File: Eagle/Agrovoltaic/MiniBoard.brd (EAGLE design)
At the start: 160 x 100 mm, 56 parts, among them J1 WAGO-03BE, J2 WAGO-03BE, J3 WAGO-03BE, K1 SRD-05VDC-SL-C, K3 SRD-05VDC-SL-C, Q1 BC338, Q2 BC338

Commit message: EDIT:Mengedit Board
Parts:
- removed CA3: 100n, rcl:E3,5-8
- removed MC1: DEVKIT_V1_ESP32-WROOM-32, DEVKIT_V1_ESP32-WROOM-32:MODULE_DEVKIT_V1_ESP32-WROOM-32
- added ANALOG, DIGITAL-IN, DIGITAL-OUT: (no value), con-wago-500:W237-102
- added CA4: 100n, rcl:E3,5-8
- added U$1: CP8-ADJ, userlib:CP8-ADJ
- added U1: ESP32-DEVKIT-V1, ESP32-DEVKIT-V1:MODULE_ESP32_DEVKIT_V1
- added UART2: 332-02, con-garry:332-02
- R12, R14: value 3K -> 2K
- R25, R26: value 3K -> 180
- moved K3 199.5 mm to (88.9, 125.7)
- moved K1 194.1 mm to (88.9, 142.2)
- moved OK3 187.4 mm to (88.9, 16.5), turned to 270 degrees
- moved R19 182.3 mm to (73.7, 26.7), turned to 180 degrees
- moved D14 177.6 mm to (87.6, 34.3), turned to 180 degrees
- moved J3 174.3 mm to (104.1, 120.7), turned to 90 degrees
- moved DZA1 165.6 mm to (73.7, 78.7)
- moved J2 163.7 mm to (104.1, 137.2), turned to 90 degrees
- moved CA2 161.6 mm to (86.4, 104.1)
- moved R14 158.8 mm to (76.2, 58.4), turned to 180 degrees
- moved I2C 155.6 mm to (57.1, 5.08)
- moved RA13 154.3 mm to (67.3, 88.9)
- moved D13 154.0 mm to (73.7, 30.5), turned to 180 degrees
- moved D3 153.5 mm to (71.1, 119.4)
- moved R1 152.9 mm to (73.7, 14.0), turned to 180 degrees
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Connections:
- removed net IO16: MC1.27
- removed net IO17: MC1.28
- removed net IO4: MC1.26
- removed net N$10: IOESP.4
- removed net N$11: IOESP.5
- removed net N$12: IOESP.6
- removed net N$13: IOESP.7
- removed net N$14: IOESP.8
- removed net N$23: CA3.+, MC1.2
- removed net N$44: MC1.16
- removed net N$45: MC1.17
- removed net N$46: MC1.18
- removed net N$5: IOESP.1
- removed net N$61: MC1.25
- removed net N$64: MC1.22
- removed net N$65: MC1.21
- removed net N$66: MC1.20
- removed net N$8: IOESP.2
- removed net N$9: IOESP.3
- removed net R3: MC1.13
- removed net R4: MC1.15
- removed net S3: MC1.9
- removed net S4: MC1.10
- new net AI2: ANALOG.2, CA2.+, DZA3.A, DZA4.C, RA21.2
- new net D12: IOESP.3, U1.27
- new net D13: IOESP.4, U1.28
- new net D25: IOESP.5, U1.23
- new net D26: IOESP.6, U1.24
- new net D4: IOESP.1, U1.5
- new net D5: IOESP.2, U1.8
- new net N$25: CA4.+, U1.16
- new net RX2: U1.6, UART2.2
- new net TX2: U1.7, UART2.1
- net 12V: now also J1.3, U$1.IN+; no longer J1.1
- net 3V3: now also U1.1; no longer MC1.1
- net 5V: now also U$1.OUT+, U1.30; no longer MC1.19
- net A1: now also U1.21; no longer MC1.7, RA21.1, RA22.2, RA23.2
- net A2: now also RA21.1, RA22.2, RA23.2, U1.22; no longer MC1.8
- net AI1: now also ANALOG.1; no longer CA2.+, DZA3.A, DZA4.C, RA21.2
- net CS: no longer MC1.29
- net GND: now also CA4.-, J1.1, U$1.IN-, U$1.OUT-, U1.2, U1.29; no longer CA3.-, J1.3, MC1.14, MC1.32, MC1.38
- net IN1: now also DIGITAL-IN.1
- net IN2: now also DIGITAL-IN.2
- net MISO: now also U1.10; no longer MC1.31
- net MOSI: now also U1.15; no longer MC1.37
- net OUT1: now also DIGITAL-OUT.1
- net OUT2: now also DIGITAL-OUT.2
- net R1: now also U1.25; no longer MC1.11
- net R2: now also U1.26; no longer MC1.12
- net RR1: now also U1.3; no longer MC1.23
- net RR2: now also U1.4; no longer MC1.24
- net RX0: now also U1.12; no longer MC1.34
- net S1: now also U1.19; no longer MC1.5
- net S2: now also U1.20; no longer MC1.6
- net SCK: now also U1.9; no longer MC1.30
- net SCL: now also U1.14; no longer MC1.36
- net SDA: now also U1.11; no longer MC1.33
- net TX0: now also U1.13; no longer MC1.35
- net VN: now also IOESP.8, U1.18; no longer MC1.4
- net VP: now also IOESP.7, U1.17; no longer MC1.3
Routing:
- net RX0: track 0.00 -> 2.81 mm
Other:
- board size 160 x 100 mm -> 108 x 151.1 mm

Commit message: EDIT:Melanjutkan
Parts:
- added SV1, SV2, SV3, SV4, SV5, SV6, SV7, SV8: (no value), con-lsta:FE10
- moved UART 40.3 mm to (55.9, 41.9), turned to 180 degrees
- moved UART2 29.8 mm to (55.9, 26.7), turned to 180 degrees
- moved R13 24.4 mm to (50.8, 82.5), turned to 270 degrees
- moved R26 24.3 mm to (33.0, 83.8)
- moved OK7 24.2 mm to (43.2, 82.5)
- moved OLED_LCD 23.0 mm to (26.7, 73.7), turned to 270 degrees
- moved CA4 19.1 mm to (29.2, 40.6), turned to 270 degrees
- moved U1 17.8 mm to (33.0, 27.9)
- moved R25 16.7 mm to (33.0, 63.5)
- moved OK6 16.6 mm to (43.2, 62.2)
- moved SPI 15.3 mm to (55.9, 16.5)
- moved R11 13.3 mm to (50.8, 62.2), turned to 90 degrees
- moved R20 7.73 mm to (72.4, 41.9)
- moved RA22 7.62 mm to (59.7, 108.0)
- moved RA23 7.62 mm to (59.7, 101.6)
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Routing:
- net 5V: track 0.00 -> 246.8 mm
- net GND: track 0.00 -> 246.5 mm
- net AI1: track 0.00 -> 43.6 mm
- net N$6: track 0.00 -> 42.7 mm
- net N$3: track 0.00 -> 42.5 mm
- net AI2: track 0.00 -> 41.3 mm
- net N$19: track 0.00 -> 26.5 mm
- net OUT2: track 0.00 -> 25.8 mm
- net COM2: track 0.00 -> 23.3 mm
- net COM1: track 0.00 -> 23.3 mm
- net 12V: track 0.00 -> 18.6 mm
- net N$4: track 0.00 -> 18.0 mm
- net OUT1: track 0.00 -> 17.3 mm
- net N$7: track 0.00 -> 16.7 mm
- net N$25: track 0.00 -> 11.2 mm
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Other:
- board text added: "Button"

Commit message: Still Edit
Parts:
- added RA1, RA2, RA3, RA4, RA5: 10K, rcl:0207/10
- added S1, S2, S3: FSM103A, FSM103A:SW_1571627-1
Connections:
- new net N$5: RA1.2, RA5.1, S1.1, S1.2
- new net N$8: RA1.1, RA2.2, S2.1, S2.2
- new net N$9: RA2.1, RA3.2, S3.1, S3.2
- net 3V3: now also RA5.2
- net CS: now also U1.8
- net D4: now also RA4.2, S1.3, S1.4, S2.3, S2.4, S3.3, S3.4
- net D5: no longer U1.8
- net GND: now also RA3.1, RA4.1
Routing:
- net SCL: track 0.00 -> 53.4 mm
- net SDA: track 0.00 -> 46.6 mm
- net N$8: track 0.00 -> 33.0 mm
- net MISO: track 0.00 -> 30.4 mm
- net D4: track 0.00 -> 29.9 mm
- net SCK: track 0.00 -> 27.2 mm
- net N$5: track 0.00 -> 23.8 mm
- net N$9: track 0.00 -> 22.7 mm
- net 12V: track 18.6 -> 40.6 mm
- net GND: track 246.5 -> 266.6 mm
- net N$19: track 26.5 -> 38.1 mm
- net RX2: track 0.00 -> 10.4 mm
- net RX0: track 0.00 -> 10.4 mm
- net TX2: track 0.00 -> 10.2 mm
- net TX0: track 0.39 -> 10.5 mm
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
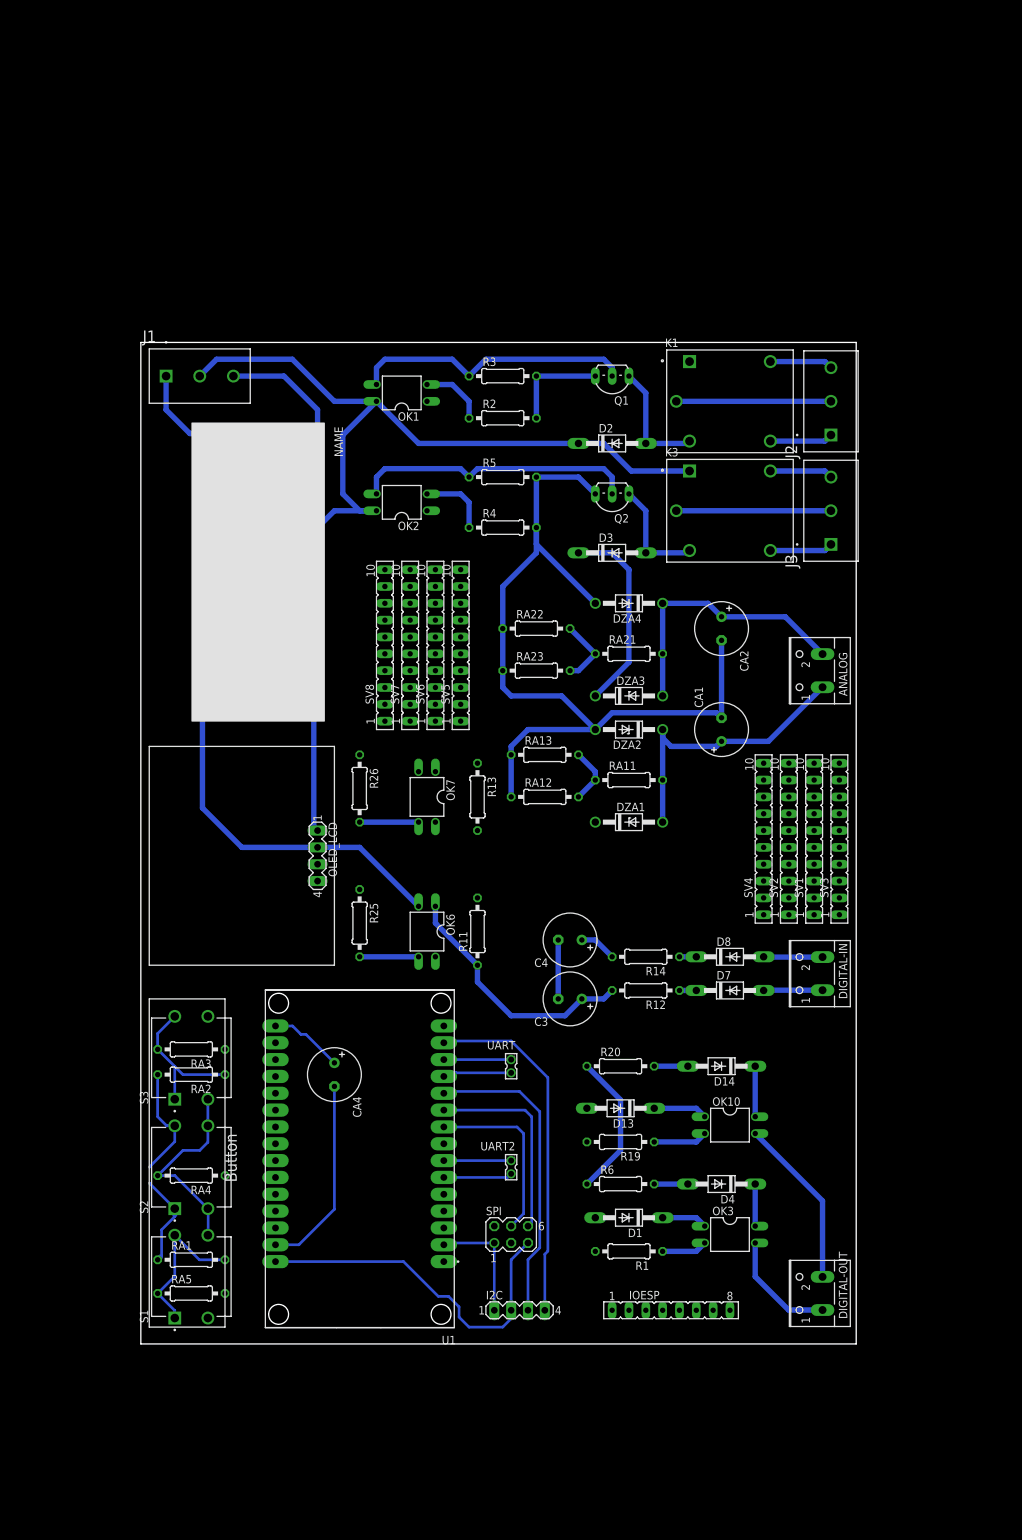
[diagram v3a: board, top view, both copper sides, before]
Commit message: rapihin beberapa bagian, agar mudah diwire
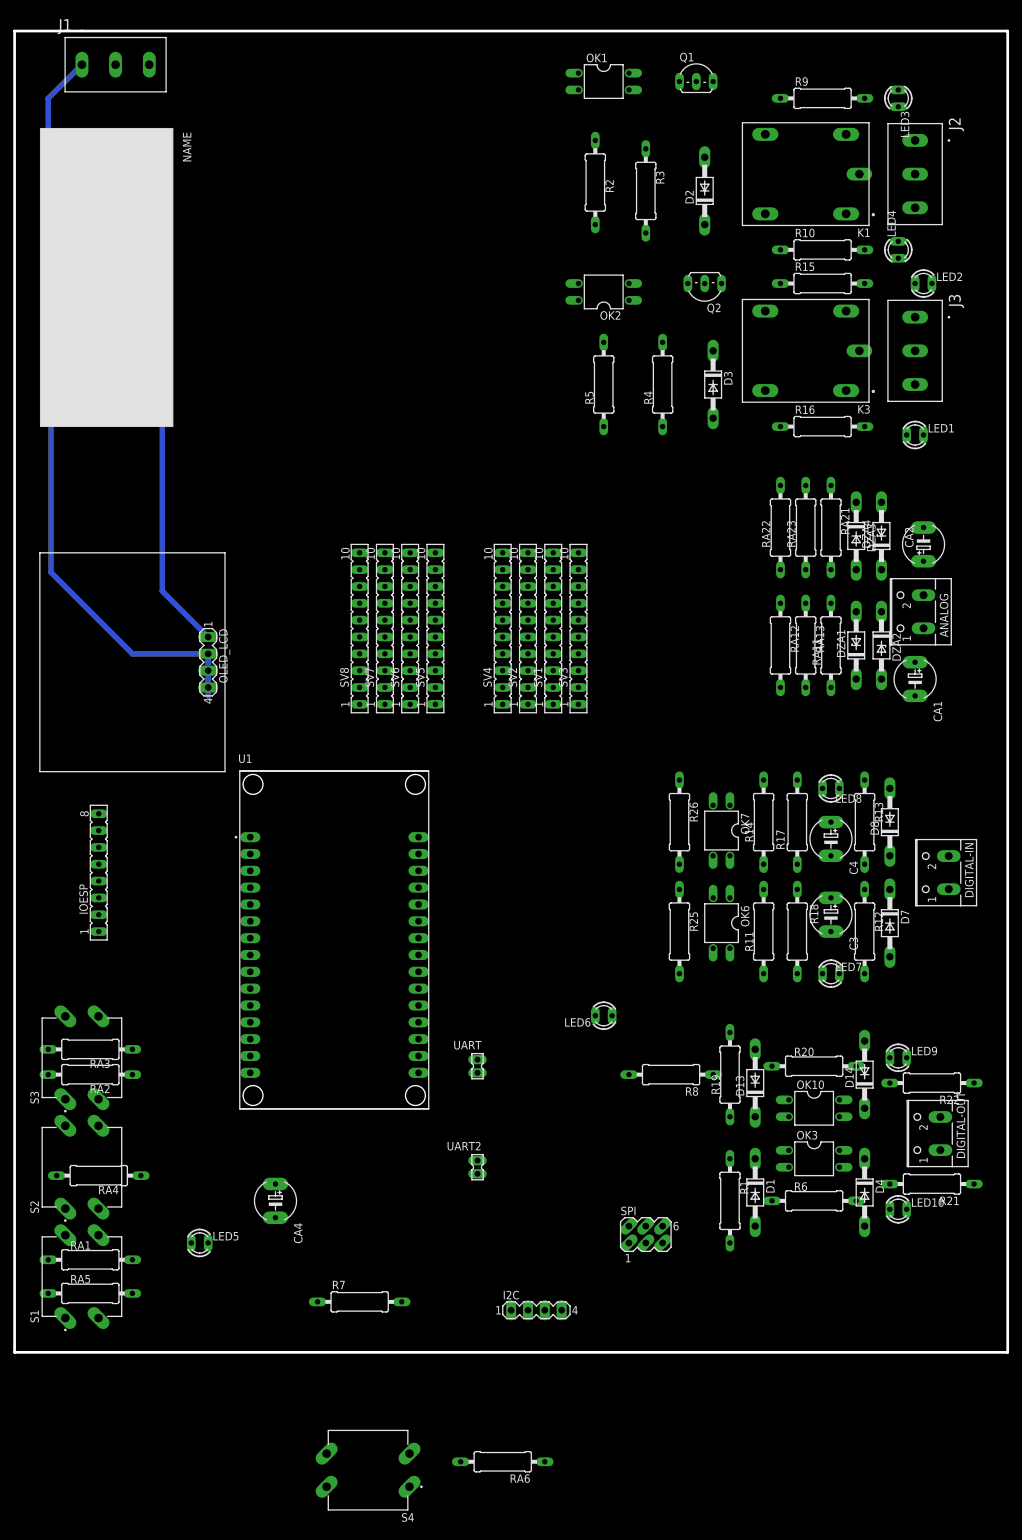
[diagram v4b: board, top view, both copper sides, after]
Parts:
- added LED1, LED10, LED2, LED3, LED4, LED5, LED6, LED7, LED8, LED9: (no value), led_WS:LED3MM
- added R10, R15, R16, R17, R18, R21, R22, R7, R8, R9: (no value), rcl-ws:0309/12
- added RA6: 10K, rcl-ws:0309/12
- added S4: FSM103A, FSM103A:SW_1571627-1
- C3, C4, CA1, CA2, CA4: device rcl:E3,5-8 -> rcl-ws:E5-6
- DZA1, DZA2, DZA3, DZA4: device diode:DO41Z10 -> diode-ws:DO41Z10
- R1, R11, R12, R13, R14, R19, R2, R20, R25, R26, R3, R4, R5, R6, RA1, RA11, RA12, RA13, RA2, RA21, RA22, RA23, RA3, RA4, RA5: device rcl:0207/10 -> rcl-ws:0309/12
- SPI: device con-lstb:MA03-2 -> con-lstb-ws:MA03-2
- UART, UART2: device con-garry:332-02 -> con-garry-ws:332-02
- moved IOESP 108.7 mm to (-6.35, 71.1), turned to 90 degrees
- moved R13 58.5 mm to (109.2, 78.7)
- moved OK1 56.0 mm to (69.8, 190.5), turned to 270 degrees
- moved SV1 50.6 mm to (62.2, 108.0)
- moved SV2 50.6 mm to (58.4, 108.0)
- moved SV4 50.6 mm to (54.6, 108.0)
- moved SV3 50.6 mm to (66.0, 108.0)
- moved U$1 50.0 mm to (-3.81, 160.0)
- moved Q1 48.7 mm to (83.8, 191.8), turned to 0 degrees
- moved J1 48.7 mm to (-8.89, 193.0)
- moved R26 48.5 mm to (81.3, 78.7)
- moved R25 48.3 mm to (81.3, 62.2)
- moved J2 46.2 mm to (116.8, 181.6), turned to 270 degrees
- moved RA23 46.0 mm to (100.3, 123.2), turned to 90 degrees
- moved OK7 44.7 mm to (87.6, 77.5)
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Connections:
- new net N$10: LED2.A, R15.2
- new net N$11: LED1.A, R16.2
- new net N$12: LED3.A, R9.2
- new net N$13: LED4.A, R10.2
- new net N$14: LED6.A, R8.2
- new net N$23: LED5.A, R7.1
- new net N$24: LED8.A, R17.2
- new net N$29: LED7.A, R18.2
- new net N$30: LED10.A, R21.2
- new net N$31: LED9.A, R22.2
- new net N$32: RA5.2, RA6.1, S4.1, S4.2
- net 12V: now also R8.1
- net 3V3: no longer RA5.2
- net 5V: now also R7.2
- net D4: now also S4.3, S4.4
- net GND: now also LED1.K, LED10.K, LED2.K, LED3.K, LED4.K, LED5.K, LED6.K, LED7.K, LED8.K, LED9.K
- net N$19: now also R18.1
- net N$21: now also R17.1
- net NC1: now also R10.1
- net NC2: now also R16.1
- net NO1: now also R9.1
- net NO2: now also R15.1
- net OUT1: now also R21.1
- net OUT2: now also R22.1
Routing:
- net 5V: track 243.7 -> 36.2 mm
- net GND: track 266.6 -> 114.0 mm
- net SCL: track 53.4 -> 0.00 mm
- net SDA: track 46.6 -> 0.00 mm
- net AI1: track 43.6 -> 0.00 mm
- net N$6: track 42.7 -> 0.00 mm
- net N$3: track 42.5 -> 0.00 mm
- net AI2: track 41.3 -> 0.00 mm
- net 12V: track 40.6 -> 0.00 mm
- net N$19: track 38.1 -> 0.00 mm
- net N$8: track 33.0 -> 0.00 mm
- net MISO: track 30.4 -> 0.00 mm
- net D4: track 29.9 -> 0.11 mm
- net SCK: track 27.2 -> 0.00 mm
- net OUT2: track 25.8 -> 0.00 mm
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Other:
- board size 108 x 151.1 mm -> 149.9 x 199.4 mm
- board text removed: "Button"

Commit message: MODIFY:Memisahkan Space Board
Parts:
- removed LED1, LED10, LED2, LED3, LED4, LED5, LED6, LED7, LED8, LED9: (no value), led_WS:LED3MM
- removed R17, R18, R7, R8: (no value), rcl-ws:0309/12
- removed R20, R6: 220, rcl-ws:0309/12
- removed SV1, SV2, SV3, SV4, SV5, SV6, SV7, SV8: (no value), con-lsta:FE10
- added L12, L5, LI1, LI2, LNC1, LNC2, LNO1, LNO2, LO1, LO2: (no value), led_WS:LED3MM
- added RL12, RL5, RLI1, RLI2: (no value), rcl-ws:0309/12
- moved J1 182.5 mm to (8.89, 11.4), turned to 90 degrees
- moved IOESP 175.5 mm to (168.9, 62.2), turned to 180 degrees
- moved U$1 149.5 mm to (38.1, 16.5), turned to 0 degrees
- moved U1 142.7 mm to (168.9, 31.8), turned to 180 degrees
- moved I2C 139.0 mm to (193.0, 44.5), turned to 90 degrees
- moved RA1 138.4 mm to (130.8, 12.7), turned to 270 degrees
- moved UART 135.9 mm to (186.7, 45.7)
- moved UART2 135.9 mm to (186.7, 30.5)
- moved R21 132.2 mm to (188.0, 137.2), turned to 90 degrees
- moved RA2 130.9 mm to (121.9, 21.6)
- moved S1 129.5 mm to (120.7, 11.4), turned to 180 degrees
- moved CA4 128.3 mm to (148.6, 21.6)
- moved D4 126.5 mm to (182.9, 125.7), turned to 0 degrees
- moved R1 124.4 mm to (184.2, 101.6), turned to 0 degrees
- moved D1 123.1 mm to (182.9, 106.7), turned to 0 degrees
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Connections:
- removed net N$17: D4.A, R6.2
- removed net N$28: D14.A, R20.2
- net 12V: now also D14.A, D2.C, D3.C, D4.A, K1.A1, K3.A1, OK1.4, OK2.4, RL12.1; no longer R20.1, R6.1, R8.1
- net 3V3: now also RA6.2
- net 5V: now also RL5.2; no longer D2.C, D3.C, K1.A1, K3.A1, OK1.4, OK2.4, R7.2
- net D4: now also RA1.2; no longer RA4.2
- net GND: now also L12.K, L5.K, LI1.K, LI2.K, LNC1.K, LNC2.K, LNO1.K, LNO2.K, LO1.K, LO2.K, RA1.1, RA2.1; no longer LED1.K, LED10.K, LED2.K, LED3.K, LED4.K, LED5.K, LED6.K, LED7.K, LED8.K, LED9.K, RA3.1, RA4.1
- net N$10: now also LNO2.A; no longer LED2.A
- net N$11: now also LNC2.A; no longer LED1.A
- net N$12: now also LNO1.A; no longer LED3.A
- net N$13: now also LNC1.A; no longer LED4.A
- net N$14: now also L12.A, RL12.2; no longer LED6.A, R8.2
- net N$19: now also RLI1.1; no longer R18.1
- net N$21: now also RLI2.1; no longer R17.1
- net N$23: now also L5.A, RL5.1; no longer LED5.A, R7.1
- net N$24: now also LI2.A, RLI2.2; no longer LED8.A, R17.2
- net N$29: now also LI1.A, RLI1.2; no longer LED7.A, R18.2
- net N$30: now also LO1.A; no longer LED10.A
- net N$31: now also LO2.A; no longer LED9.A
- net N$5: now also RA4.2, S3.1, S3.2; no longer RA1.2, S1.1, S1.2
- net N$8: now also RA3.2, RA4.1; no longer RA1.1, RA2.2
- net N$9: now also RA2.2, RA3.1, S1.1, S1.2; no longer RA2.1, RA3.2, S3.1, S3.2
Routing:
- net GND: track 114.0 -> 441.2 mm, vias 0 -> 3
- net D4: track 0.11 -> 196.8 mm, vias 0 -> 1
- net 5V: track 36.2 -> 174.4 mm, vias 0 -> 3
- net 12V: track 0.00 -> 102.4 mm, vias 0 -> 1
- net N$32: track 0.00 -> 94.0 mm
- net D12: track 0.00 -> 75.2 mm
- net D25: track 0.00 -> 51.1 mm
- net N$7: track 0.00 -> 40.1 mm
- net N$4: track 0.00 -> 38.8 mm
- net NC2: track 0.00 -> 38.1 mm
- net NO2: track 0.00 -> 36.9 mm
- net NO1: track 0.00 -> 36.9 mm
- net NC1: track 0.00 -> 36.2 mm
- net MOSI: track 0.00 -> 35.8 mm
- net N$5: track 0.00 -> 34.8 mm
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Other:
- board size 149.9 x 199.4 mm -> 199.4 x 149.9 mm
- board text added: "BUTTON"
- board text added: "CUSTOM SPACE"
- board text added: "DISPLAY SPACE"
- board text added: "ISOLATION SPACE"
- board text added: "MICROCONTROLLER"
- board text added: "POWER DISTRIBUTION"

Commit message: FINISHING
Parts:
- removed IOESP: (no value), con-lsta:FE08
- moved R4 15.3 mm to (61.0, 96.5), turned to 90 degrees
- moved CA4 15.2 mm to (163.8, 21.6)
- moved OK2 14.8 mm to (50.8, 96.5)
- moved OK1 13.7 mm to (19.1, 96.5)
- moved R2 13.7 mm to (27.9, 96.5), turned to 90 degrees
- moved R3 6.84 mm to (17.8, 86.4)
- moved R5 6.48 mm to (49.5, 86.4)
- moved RA13 6.35 mm to (96.5, 113.0)
- moved RA23 6.35 mm to (76.2, 113.0)
- moved RA12 5.08 mm to (96.5, 119.4)
- moved RA22 5.08 mm to (76.2, 119.4)
- moved OK3 4.02 mm to (181.6, 115.6)
- moved Q2 3.81 mm to (41.9, 100.3), turned to 270 degrees
- moved OK10 2.84 mm to (167.6, 115.6)
- moved Q1 2.54 mm to (10.2, 100.3), turned to 270 degrees
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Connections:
- removed net D5: IOESP.2
- net D12: no longer IOESP.3
- net D13: no longer IOESP.4
- net D25: no longer IOESP.5
- net D26: no longer IOESP.6
- net D4: no longer IOESP.1
- net VN: no longer IOESP.8
- net VP: no longer IOESP.7
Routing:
- net GND: track 441.2 -> 1207.4 mm, vias 3 -> 14
- net 5V: track 174.4 -> 615.3 mm, vias 3 -> 8
- net 12V: track 102.4 -> 481.1 mm, vias 1 -> 7
- net RR1: track 6.74 -> 239.4 mm, vias 0 -> 2
- net A2: track 18.1 -> 232.9 mm, vias 0 -> 2
- net RR2: track 6.74 -> 207.6 mm, vias 0 -> 2
- net 3V3: track 8.15 -> 199.0 mm, vias 1 -> 2
- net A1: track 19.3 -> 208.2 mm, vias 0 -> 4
- net S2: track 5.35 -> 186.1 mm, vias 0 -> 2
- net R2: track 18.0 -> 163.9 mm, vias 0 -> 3
- net S1: track 5.36 -> 143.6 mm, vias 0 -> 4
- net D4: track 196.8 -> 305.5 mm, vias 1 -> 2
- net SDA: track 27.3 -> 130.7 mm, vias 1 -> 2
- net R1: track 14.9 -> 113.1 mm, vias 0 -> 2
- net SCL: track 29.1 -> 122.9 mm, vias 1 -> 2
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
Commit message: ADD: Logo
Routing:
- added copper zone on layer 16, net GND
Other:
- board text added: "ISOESP32 VER 0.1 AGROVOLTAIC BY ALMUZKY & SALMAN"

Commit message: REV:Revisi rangkaian 1
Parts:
- RA11, RA21: value 10K -> 100K
- RA12, RA22: value 100K -> 10K
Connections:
- removed net N$49: OK6.3, R25.2
- removed net N$50: OK7.3, R26.2
- net GND: now also R10.2, R15.2, R16.2, R21.2, R22.2, R25.1, R26.1, R9.2; no longer LNC1.K, LNC2.K, LNO1.K, LNO2.K, LO1.K, LO2.K
- net N$10: now also LNO2.K, R15.1; no longer LNO2.A, R15.2
- net N$11: now also LNC2.K, R16.1; no longer LNC2.A, R16.2
- net N$12: now also LNO1.K, R9.1; no longer LNO1.A, R9.2
- net N$13: now also LNC1.K, R10.1; no longer LNC1.A, R10.2
- net N$30: now also LO1.K, R21.1; no longer LO1.A, R21.2
- net N$31: now also LO2.K, R22.1; no longer LO2.A, R22.2
- net NC1: now also LNC1.A; no longer R10.1
- net NC2: now also LNC2.A; no longer R16.1
- net NO1: now also LNO1.A; no longer R9.1
- net NO2: now also LNO2.A; no longer R15.1
- net OUT1: now also LO1.A; no longer R21.1
- net OUT2: now also LO2.A; no longer R22.1
- net S1: now also OK6.3, R25.2; no longer R25.1
- net S2: now also OK7.3, R26.2; no longer R26.1
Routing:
- net GND: track 1207.4 -> 1166.8 mm, vias 14 -> 15
- net S1: track 143.6 -> 124.7 mm, vias 4 -> 3
- net N$11: track 15.0 -> 0.00 mm
- net N$10: track 15.0 -> 0.00 mm
- net N$49: track 14.8 -> 0.00 mm
- net N$13: track 14.0 -> 0.00 mm
- net N$12: track 14.0 -> 0.00 mm
- net OUT1: track 42.9 -> 32.7 mm
- net OUT2: track 40.4 -> 31.2 mm
- net NC1: track 36.2 -> 27.6 mm
- net NO2: track 36.9 -> 31.3 mm
- net NO1: track 36.9 -> 31.3 mm
- net N$50: track 5.61 -> 0.00 mm
- net N$31: track 5.08 -> 0.00 mm
- net N$30: track 5.08 -> 0.00 mm
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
